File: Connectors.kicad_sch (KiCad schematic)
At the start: 4 parts, among them J1 Conn_01x04_Pin, J2 Conn_01x04_Pin, J3 Conn_02x03_Odd_Even, J4 Conn_01x09_Pin

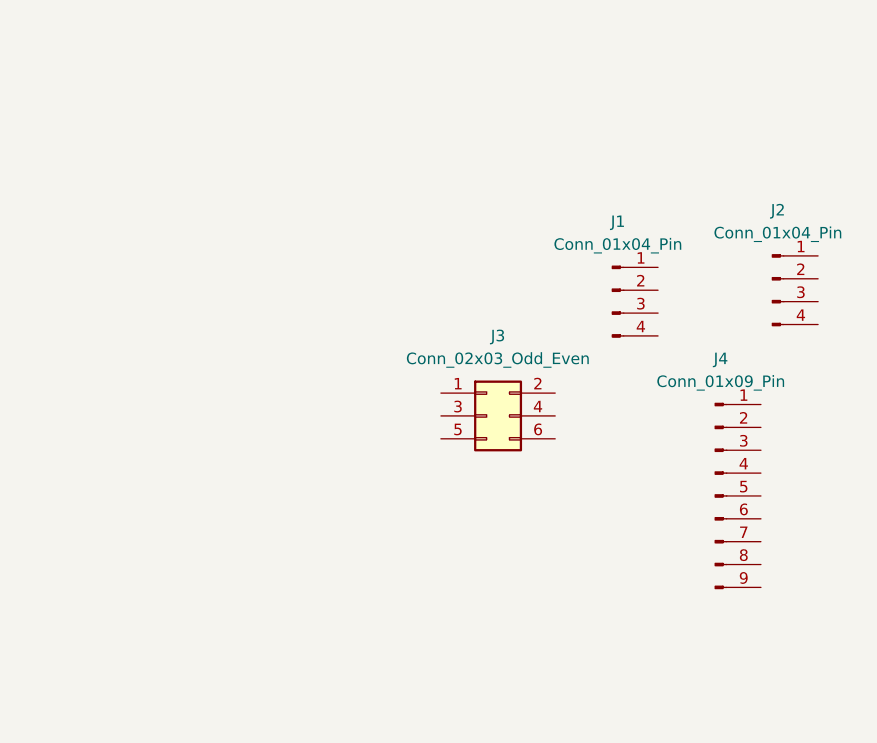
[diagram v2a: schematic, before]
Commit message: Allocated GND and Vcc Nets to the power net class
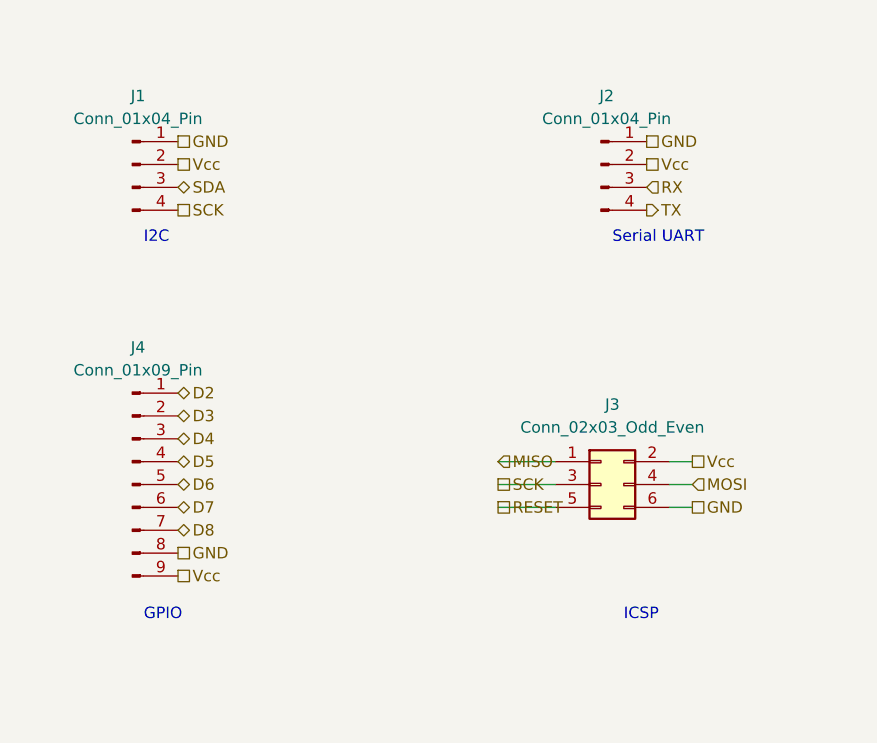
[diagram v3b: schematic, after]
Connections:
- net GND: now reaches J1.1 (Pin_1)
- net GND: now also J2.1 (Pin_1), J3.6 (Pin_6), J4.8 (Pin_8)
- net Vcc: now reaches J1.2 (Pin_2)
- net Vcc: now also J2.2 (Pin_2), J3.2 (Pin_2), J4.9 (Pin_9)
- net SDA: now reaches J1.3 (Pin_3)
- net SCK: now reaches J1.4 (Pin_4)
- net SCK: now also J3.3 (Pin_3)
- net D2: now reaches J4.1 (Pin_1)
- net D3: now reaches J4.2 (Pin_2)
- net D4: now reaches J4.3 (Pin_3)
- net D5: now reaches J4.4 (Pin_4)
- net D6: now reaches J4.5 (Pin_5)
- net D7: now reaches J4.6 (Pin_6)
- net D8: now reaches J4.7 (Pin_7)
- net MISO: now reaches J3.1 (Pin_1)
- net MOSI: now reaches J3.4 (Pin_4)
- net RESET: now reaches J3.5 (Pin_5)
- net RX: now reaches J2.3 (Pin_3)
- net TX: now reaches J2.4 (Pin_4)
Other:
- note added: "GPIO"
- note added: "I2C"
- note added: "ICSP"
- note added: "Serial UART"
- moved on the sheet: J1, J2, J3, J4
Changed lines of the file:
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@@
 (kicad_sch (version 20230121) (generator eeschema)
   (paper "A4")
-  (symbol (lib_id "Connector:Conn_01x04_Pin") (at 166.37 90.17 0) (unit 1)
-    (in_bom yes) (on_board yes) (dnp no) (fields_autoplaced)
-    (property "Reference" "J1" (at 167.005 82.55 0)
-      (effects (font (size 1.27 1.27)))
-    )
-    (property "Value" "Conn_01x04_Pin" (at 167.005 85.09 0)
-      (effects (font (size 1.27 1.27)))
-    )
-    (property "Footprint" "Connector_PinHeader_2.54mm:PinHeader_1x04_P2.54mm_Vertical" (at 166.37 90.17 0)
-      (effects (font (size 1.27 1.27)) hide)
-    )
-    (property "Datasheet" "~" (at 166.37 90.17 0)
+  (wire (pts (xy 175.26 111.76) (xy 172.72 111.76))
+    (stroke (width 0) (type default))
+  )
+  (wire (pts (xy 153.67 111.76) (xy 160.02 111.76))
+    (stroke (width 0) (type default))
+  )
+  (wire (pts (xy 153.67 114.3) (xy 160.02 114.3))
+    (stroke (width 0) (type default))
+  )
+  (wire (pts (xy 172.72 109.22) (xy 175.26 109.22))
+    (stroke (width 0) (type default))
+  )
+  (wire (pts (xy 153.67 109.22) (xy 160.02 109.22))
+    (stroke (width 0) (type default))
+  )
+  (wire (pts (xy 172.72 114.3) (xy 175.26 114.3))
+    (stroke (width 0) (type default))
+  )
+  (text "ICSP" (at 167.64 127 0)
+    (effects (font (size 1.27 1.27)) (justify left bottom))
+  )
+  (text "GPIO\n" (at 114.3 127 0)
+    (effects (font (size 1.27 1.27)) (justify left bottom))
+  )
+  (text "Serial UART" (at 166.37 85.09 0)
+    (effects (font (size 1.27 1.27)) (justify left bottom))
+  )
+  (text "I2C\n" (at 114.3 85.09 0)
+    (effects (font (size 1.27 1.27)) (justify left bottom))
+  )
+  (hierarchical_label "Vcc" (shape passive) (at 118.11 76.2 0) (fields_autoplaced)
+    (effects (font (size 1.27 1.27)) (justify left))
+  )
+  (hierarchical_label "MOSI" (shape input) (at 175.26 111.76 0) (fields_autoplaced)
+    (effects (font (size 1.27 1.27)) (justify left))
+  )
+  (hierarchical_label "D3" (shape bidirectional) (at 118.11 104.14 0) (fields_autoplaced)
+    (effects (font (size 1.27 1.27)) (justify left))
+  )
+  (hierarchical_label "GND" (shape passive) (at 118.11 73.66 0) (fields_autoplaced)
+    (effects (font (size 1.27 1.27)) (justify left))
+  )
+  (hierarchical_label "D5" (shape bidirectional) (at 118.11 109.22 0) (fields_autoplaced)
+    (effects (font (size 1.27 1.27)) (justify left))
+  )
+  (hierarchical_label "GND" (shape passive) (at 175.26 114.3 0) (fields_autoplaced)
+    (effects (font (size 1.27 1.27)) (justify left))
+  )
+  (hierarchical_label "RESET" (shape passive) (at 153.67 114.3 0) (fields_autoplaced)
+    (effects (font (size 1.27 1.27)) (justify left))
+  )
+  (hierarchical_label "SCK" (shape passive) (at 153.67 111.76 0) (fields_autoplaced)
+    (effects (font (size 1.27 1.27)) (justify left))
+  )
+  (hierarchical_label "GND" (shape passive) (at 170.18 73.66 0) (fields_autoplaced)
+    (effects (font (size 1.27 1.27)) (justify left))
+  )
+  (hierarchical_label "MISO" (shape input) (at 153.67 109.22 0) (fields_autoplaced)
+    (effects (font (size 1.27 1.27)) (justify left))
+  )
+  (hierarchical_label "Vcc" (shape passive) (at 170.18 76.2 0) (fields_autoplaced)
+    (effects (font (size 1.27 1.27)) (justify left))
+  )
+  (hierarchical_label "D4" (shape bidirectional) (at 118.11 106.68 0) (fields_autoplaced)
+    (effects (font (size 1.27 1.27)) (justify left))
+  )
+  (hierarchical_label "SCK" (shape passive) (at 118.11 81.28 0) (fields_autoplaced)
+    (effects (font (size 1.27 1.27)) (justify left))
+  )
+  (hierarchical_label "D8" (shape bidirectional) (at 118.11 116.84 0) (fields_autoplaced)
+    (effects (font (size 1.27 1.27)) (justify left))
+  )
+  (hierarchical_label "D2" (shape bidirectional) (at 118.11 101.6 0) (fields_autoplaced)
+    (effects (font (size 1.27 1.27)) (justify left))
+  )
+  (hierarchical_label "D6" (shape bidirectional) (at 118.11 111.76 0) (fields_autoplaced)
+    (effects (font (size 1.27 1.27)) (justify left))
+  )
+  (hierarchical_label "SDA" (shape bidirectional) (at 118.11 78.74 0) (fields_autoplaced)
+    (effects (font (size 1.27 1.27)) (justify left))
+  )
+  (hierarchical_label "Vcc" (shape passive) (at 175.26 109.22 0) (fields_autoplaced)
+    (effects (font (size 1.27 1.27)) (justify left))
+  )
+  (hierarchical_label "TX" (shape output) (at 170.18 81.28 0) (fields_autoplaced)
+    (effects (font (size 1.27 1.27)) (justify left))
+  )
+  (hierarchical_label "GND" (shape passive) (at 118.11 119.38 0) (fields_autoplaced)
+    (effects (font (size 1.27 1.27)) (justify left))
+  )
+  (hierarchical_label "RX" (shape input) (at 170.18 78.74 0) (fields_autoplaced)
+    (effects (font (size 1.27 1.27)) (justify left))
+  )
+  (hierarchical_label "Vcc" (shape passive) (at 118.11 121.92 0) (fields_autoplaced)
+    (effects (font (size 1.27 1.27)) (justify left))
+  )
+  (hierarchical_label "D7" (shape bidirectional) (at 118.11 114.3 0) (fields_autoplaced)
+    (effects (font (size 1.27 1.27)) (justify left))
+  )
+  (symbol (lib_id "Connector:Conn_01x04_Pin") (at 113.03 76.2 0) (unit 1)
+    (in_bom yes) (on_board yes) (dnp no) (fields_autoplaced)
+    (property "Reference" "J1" (at 113.665 68.58 0)
+      (effects (font (size 1.27 1.27)))
+    )
+    (property "Value" "Conn_01x04_Pin" (at 113.665 71.12 0)
+      (effects (font (size 1.27 1.27)))
+    )
+    (property "Footprint" "Connector_PinHeader_2.54mm:PinHeader_1x04_P2.54mm_Vertical" (at 113.03 76.2 0)
+      (effects (font (size 1.27 1.27)) hide)
+    )
+    (property "Datasheet" "~" (at 113.03 76.2 0)
+      (effects (font (size 1.27 1.27)) hide)
+    )
+    (property "Description" "" (at 113.03 76.2 0)
       (effects (font (size 1.27 1.27)) hide)
     )
@@
     )
   )
-  (symbol (lib_id "Connector:Conn_01x09_Pin") (at 177.8 113.03 0) (unit 1)
-    (in_bom yes) (on_board yes) (dnp no) (fields_autoplaced)
-    (property "Reference" "J4" (at 178.435 97.79 0)
-      (effects (font (size 1.27 1.27)))
-    )
-    (property "Value" "Conn_01x09_Pin" (at 178.435 100.33 0)
-      (effects (font (size 1.27 1.27)))
-    )
-    (property "Footprint" "Connector_PinHeader_2.54mm:PinHeader_1x09_P2.54mm_Vertical" (at 177.8 113.03 0)
-      (effects (font (size 1.27 1.27)) hide)
-    )
-    (property "Datasheet" "~" (at 177.8 113.03 0)
+  (symbol (lib_id "Connector:Conn_01x09_Pin") (at 113.03 111.76 0) (unit 1)
+    (in_bom yes) (on_board yes) (dnp no) (fields_autoplaced)
+    (property "Reference" "J4" (at 113.665 96.52 0)
+      (effects (font (size 1.27 1.27)))
+    )
+    (property "Value" "Conn_01x09_Pin" (at 113.665 99.06 0)
+      (effects (font (size 1.27 1.27)))
+    )
+    (property "Footprint" "Connector_PinHeader_2.54mm:PinHeader_1x09_P2.54mm_Vertical" (at 113.03 111.76 0)
+      (effects (font (size 1.27 1.27)) hide)
+    )
+    (property "Datasheet" "~" (at 113.03 111.76 0)
       (effects (font (size 1.27 1.27)) hide)
     )
@@
     )
   )
-  (symbol (lib_id "Connector_Generic:Conn_02x03_Odd_Even") (at 152.4 104.14 0) (unit 1)
-    (in_bom yes) (on_board yes) (dnp no) (fields_autoplaced)
-    (property "Reference" "J3" (at 153.67 95.25 0)
-      (effects (font (size 1.27 1.27)))
-    )
-    (property "Value" "Conn_02x03_Odd_Even" (at 153.67 97.79 0)
-      (effects (font (size 1.27 1.27)))
-    )
-    (property "Footprint" "Connector_PinHeader_2.54mm:PinHeader_2x03_P2.54mm_Vertical" (at 152.4 104.14 0)
-      (effects (font (size 1.27 1.27)) hide)
-    )
-    (property "Datasheet" "~" (at 152.4 104.14 0)
+  (symbol (lib_id "Connector_Generic:Conn_02x03_Odd_Even") (at 165.1 111.76 0) (unit 1)
+    (in_bom yes) (on_board yes) (dnp no) (fields_autoplaced)
+    (property "Reference" "J3" (at 166.37 102.87 0)
+      (effects (font (size 1.27 1.27)))
+    )
+    (property "Value" "Conn_02x03_Odd_Even" (at 166.37 105.41 0)
+      (effects (font (size 1.27 1.27)))
+    )
+    (property "Footprint" "Connector_PinHeader_2.54mm:PinHeader_2x03_P2.54mm_Vertical" (at 165.1 111.76 0)
+      (effects (font (size 1.27 1.27)) hide)
+    )
+    (property "Datasheet" "~" (at 165.1 111.76 0)
+      (effects (font (size 1.27 1.27)) hide)
+    )
+    (property "Purpose" "" (at 165.1 111.76 0)
       (effects (font (size 1.27 1.27)) hide)
     )
@@
     )
   )
-  (symbol (lib_id "Connector:Conn_01x04_Pin") (at 184.15 88.9 0) (unit 1)
-    (in_bom yes) (on_board yes) (dnp no) (fields_autoplaced)
-    (property "Reference" "J2" (at 184.785 81.28 0)
-      (effects (font (size 1.27 1.27)))
-    )
-    (property "Value" "Conn_01x04_Pin" (at 184.785 83.82 0)
-      (effects (font (size 1.27 1.27)))
-    )
-    (property "Footprint" "Connector_PinHeader_2.54mm:PinHeader_1x04_P2.54mm_Vertical" (at 184.15 88.9 0)
-      (effects (font (size 1.27 1.27)) hide)
-    )
-    (property "Datasheet" "~" (at 184.15 88.9 0)
-      (effects (font (size 1.27 1.27)) hide)
-    )
+  (symbol (lib_id "Connector:Conn_01x04_Pin") (at 165.1 76.2 0) (unit 1)
+    (in_bom yes) (on_board yes) (dnp no) (fields_autoplaced)
+    (property "Reference" "J2" (at 165.735 68.58 0)
+      (effects (font (size 1.27 1.27)))
+    )
+    (property "Value" "Conn_01x04_Pin" (at 165.735 71.12 0)
+      (effects (font (size 1.27 1.27)))
+    )
+    (property "Footprint" "Connector_PinHeader_2.54mm:PinHeader_1x04_P2.54mm_Vertical" (at 165.1 76.2 0)
+      (effects (font (size 1.27 1.27)) hide)
+    )
+    (property "Datasheet" "~" (at 165.1 76.2 0)
+      (effects (font (size 1.27 1.27)) hide)
+    )
+    (property "Description" "" (at 165.1 76.2 0)
+      (effects (font (size 1.27 1.27)) hide)
+    )

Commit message: Completed comments
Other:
- note added: "Connectors"
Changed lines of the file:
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@@
     (stroke (width 0) (type default))
+  )
+  (rectangle (start 101.6 63.5) (end 190.5 138.43)
+    (stroke (width 0) (type default))
+    (fill (type none))
+  )
+  (text "Connectors" (at 100.33 62.23 0)
+    (effects (font (size 1.27 1.27) (thickness 0.254) bold) (justify left bottom))
   )
   (text "ICSP" (at 167.64 127 0)

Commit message: fixed bugs in schematic
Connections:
- net SCK: no longer J1.4 (Pin_4)
- new net SCL: J1.4 (Pin_4)
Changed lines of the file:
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@@
     (effects (font (size 1.27 1.27)) (justify left))
   )
-  (hierarchical_label "SCK" (shape passive) (at 118.11 81.28 0) (fields_autoplaced)
+  (hierarchical_label "SCL" (shape passive) (at 118.11 81.28 0) (fields_autoplaced)
     (effects (font (size 1.27 1.27)) (justify left))
   )
